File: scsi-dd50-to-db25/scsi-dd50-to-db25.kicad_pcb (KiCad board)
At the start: 2 copper layers, 42.8 x 70 mm, 2 parts, among them J1 DD50_Plug_MountingHoles, J2 DB25_Socket_MountingHoles

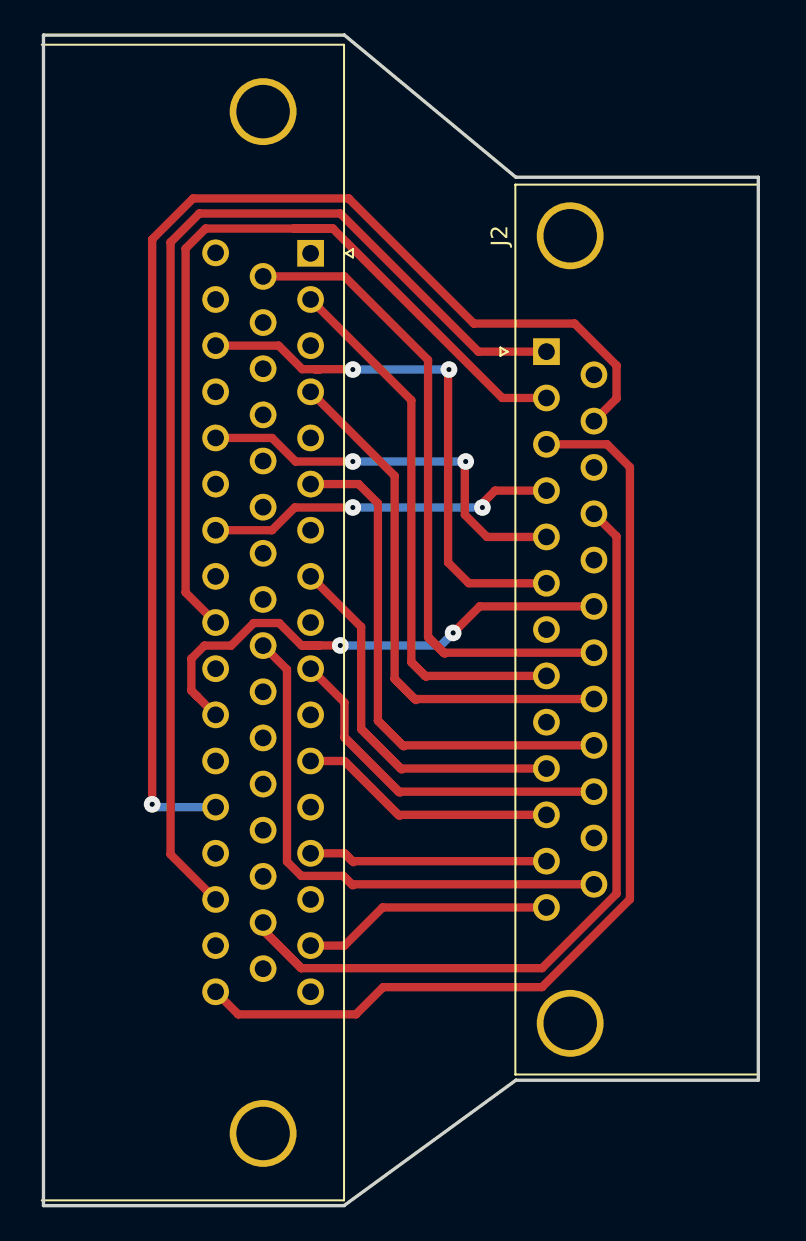
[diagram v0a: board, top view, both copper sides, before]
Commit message: Added a term power port for pulling 5v off to another adapter.
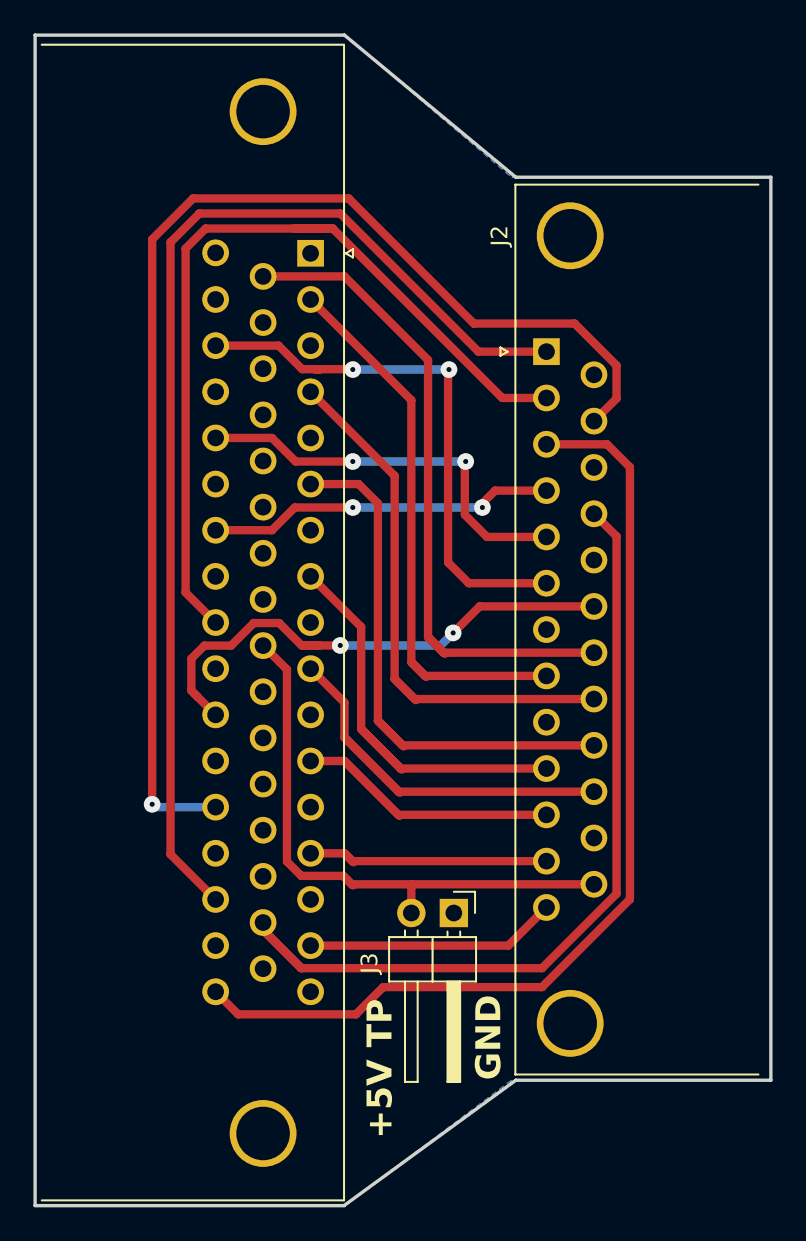
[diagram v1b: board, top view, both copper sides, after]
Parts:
- added J3: Conn_01x02, Connector_PinHeader_2.54mm:PinHeader_1x02_P2.54mm_Horizontal, F.Cu at (131.5, 105.5)
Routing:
- net /TERM_POWER: track 33.2 -> 34.9 mm
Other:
- board size 42.8 x 70 mm -> 44 x 70 mm
- board text added: "+5V TP"
- board text added: "GND"

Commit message: Fixing the pinout of the Sun Microsystems SCSI SE DD50 connector.
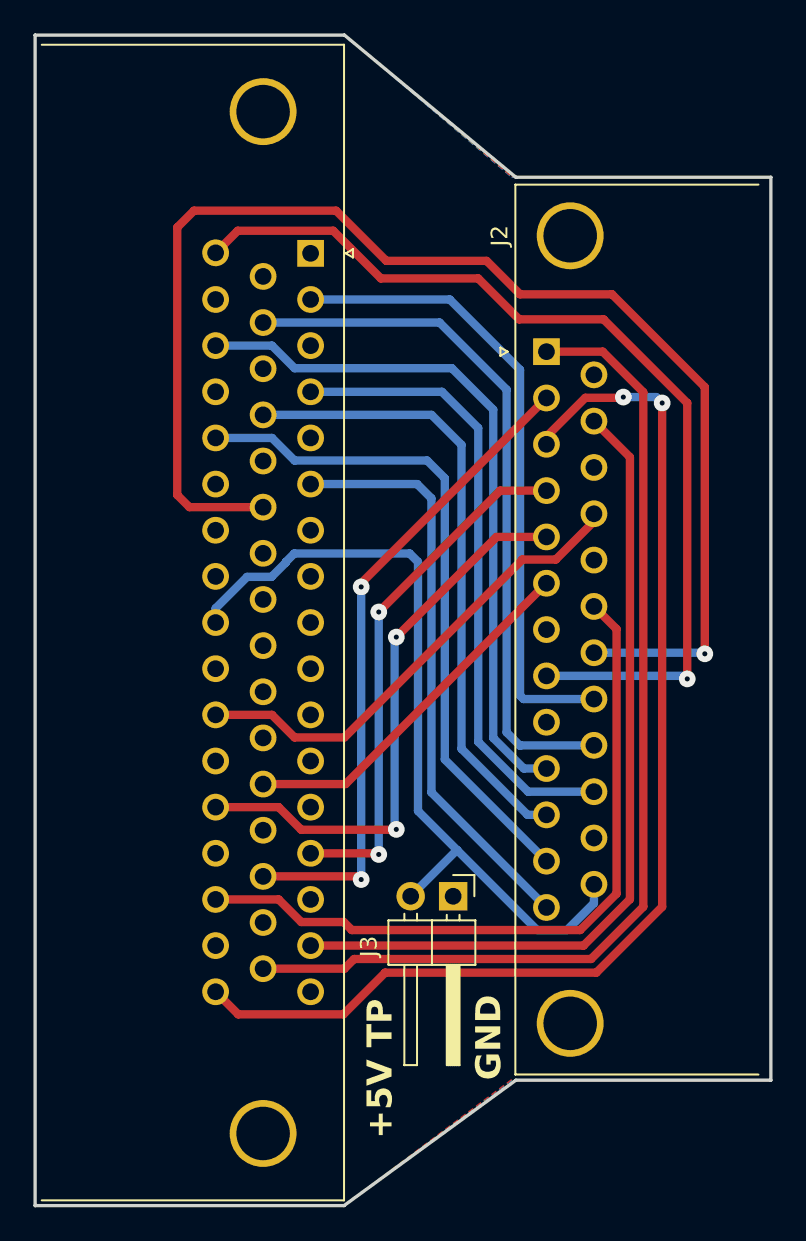
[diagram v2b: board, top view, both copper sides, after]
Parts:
- moved J3 1.00 mm to (131.5, 104.5)
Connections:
- net /IN/OUT renamed /CONN_50
- J1 pad 0: /GND -> /CONN_1
- J1 pad 1: /GND -> /CONN_1
- J1 pad 10: /DATA_BUS_4 -> /CONN_1
- J1 pad 11: /GND -> /CONN_1
- J1 pad 12: /DATA_BUS_5 -> /CONN_1
- J1 pad 13: /GND -> /CONN_1
- J1 pad 14: /DATA_BUS_6 -> /CONN_14
- J1 pad 15: /GND -> /CONN_1
- J1 pad 16: /DATA_BUS_7 -> /COMMAND/DATA
- J1 pad 17: /GND -> /CONN_1
- J1 pad 18: /DATA_BUS_PARITY -> /CONN_1
- J1 pad 19: /GND -> /CONN_19
- J1 pad 2: /DATA_BUS_0 -> /CONN_2
- J1 pad 20: /GND -> /CONN_1
- J1 pad 21: /GND -> /CONN_21
- J1 pad 22: /GND -> /CONN_1
- J1 pad 23: /GND -> /CONN_23
- J1 pad 24: /GND -> /CONN_1
- J1 pad 25: unconnected-(J1-Pad25) -> /CONN_1
- J1 pad 26: /TERM_POWER -> /CONN_1
- J1 pad 27: /GND -> /CONN_1
- J1 pad 28: /GND -> /CONN_1
- J1 pad 29: /GND -> /BUSY
- J1 pad 3: /GND -> /CONN_1
- J1 pad 30: /GND -> /CONN_1
- J1 pad 31: /GND -> /CONN_31
- J1 pad 32: /ATTENTION -> /CONN_1
- J1 pad 33: /GND -> /CONN_33
- J1 pad 34: /GND -> /CONN_34
- J1 pad 35: /GND -> /CONN_1
- J1 pad 36: /BUSY -> /CONN_36
- J1 pad 37: /GND -> /CONN_1
- J1 pad 38: /ACKNOWLEDGE -> /CONN_38
- J1 pad 39: /GND -> /CONN_1
- J1 pad 4: /DATA_BUS_1 -> /CONN_4
- J1 pad 40: /RESET -> /CONN_1
- J1 pad 41: /GND -> /CONN_1
- J1 pad 42: /MESSAGE -> /CONN_42
- J1 pad 43: /GND -> /CONN_1
- J1 pad 44: /SELECT -> /ATTENTION
- J1 pad 45: /GND -> /CONN_1
- J1 pad 46: /COMMAND/DATA -> /ACKNOWLEDGE
- J1 pad 47: /GND -> /CONN_1
- J1 pad 48: /REQUEST -> /CONN_48
- J1 pad 49: /GND -> /CONN_1
- J1 pad 5: /GND -> /CONN_1
- J1 pad 6: /DATA_BUS_2 -> /CONN_6
- J1 pad 7: /GND -> /CONN_1
- J1 pad 8: /DATA_BUS_3 -> /CONN_1
- J1 pad 9: /GND -> /CONN_9
- J2 pad 0: /GND -> /CONN_1
- J2 pad 1: /REQUEST -> /CONN_33
- J2 pad 10: /DATA_BUS_3 -> /CONN_36
- J2 pad 11: /DATA_BUS_5 -> /CONN_21
- J2 pad 12: /DATA_BUS_6 -> /CONN_38
- J2 pad 13: /DATA_BUS_7 -> /CONN_6
- J2 pad 14: /GND -> /CONN_1
- J2 pad 16: /GND -> /CONN_1
- J2 pad 18: /GND -> /CONN_1
- J2 pad 19: /SELECT -> /CONN_48
- J2 pad 2: /MESSAGE -> /CONN_31
- J2 pad 20: /DATA_BUS_PARITY -> /CONN_23
- J2 pad 21: /DATA_BUS_1 -> /CONN_2
- J2 pad 22: /DATA_BUS_2 -> /CONN_19
- J2 pad 23: /DATA_BUS_4 -> /CONN_4
- J2 pad 24: /GND -> /CONN_1
- J2 pad 25: /TERM_POWER -> /CONN_42
- J2 pad 4: /RESET -> /CONN_14
- J2 pad 7: /GND -> /CONN_1
- J2 pad 8: /DATA_BUS_0 -> /CONN_34
- J2 pad 9: /GND -> /CONN_1
- J3 pad 1: /GND -> /CONN_1
- J3 pad 2: /TERM_POWER -> /CONN_42
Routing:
- net /CONN_23: track 0.00 -> 80.4 mm, vias 0 -> 1
- net /REQUEST: track 67.0 -> 0.00 mm
- net /CONN_33: track 0.00 -> 61.8 mm
- net /CONN_34: track 0.00 -> 58.0 mm, vias 0 -> 1
- net /MESSAGE: track 51.7 -> 0.00 mm
- net /CONN_42: track 0.00 -> 48.6 mm
- net /CONN_48: track 0.00 -> 43.4 mm
- net /CONN_19: track 0.00 -> 42.3 mm
- net /CONN_36: track 0.00 -> 41.8 mm
- net /DATA_BUS_PARITY: track 40.2 -> 0.00 mm
- net /CONN_38: track 0.00 -> 40.1 mm
- net /CONN_31: track 0.00 -> 39.3 mm, vias 0 -> 2
- net /CONN_2: track 0.00 -> 38.3 mm
- net /CONN_4: track 0.00 -> 37.8 mm
- net /CONN_21: track 0.00 -> 37.5 mm
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- added copper zone on B.Cu, net /CONN_1
- added copper zone on F.Cu, net /CONN_1
- removed copper zone on B.Cu, net /GND
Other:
- board text added: "SCSI SINGLE ENDED DD50 TO DB25 2025 - v2"
- board text removed: "SCSI SINGLE ENDED DD50 TO DB25 2025 - v0.1"
